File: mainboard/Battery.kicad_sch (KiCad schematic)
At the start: 24 parts, among them IC701 USBLC6-2P6, IC702 BQ21040DBV, IC703 MAX17048, Q701 Si2333CDS, X701 USB, X702 Battery

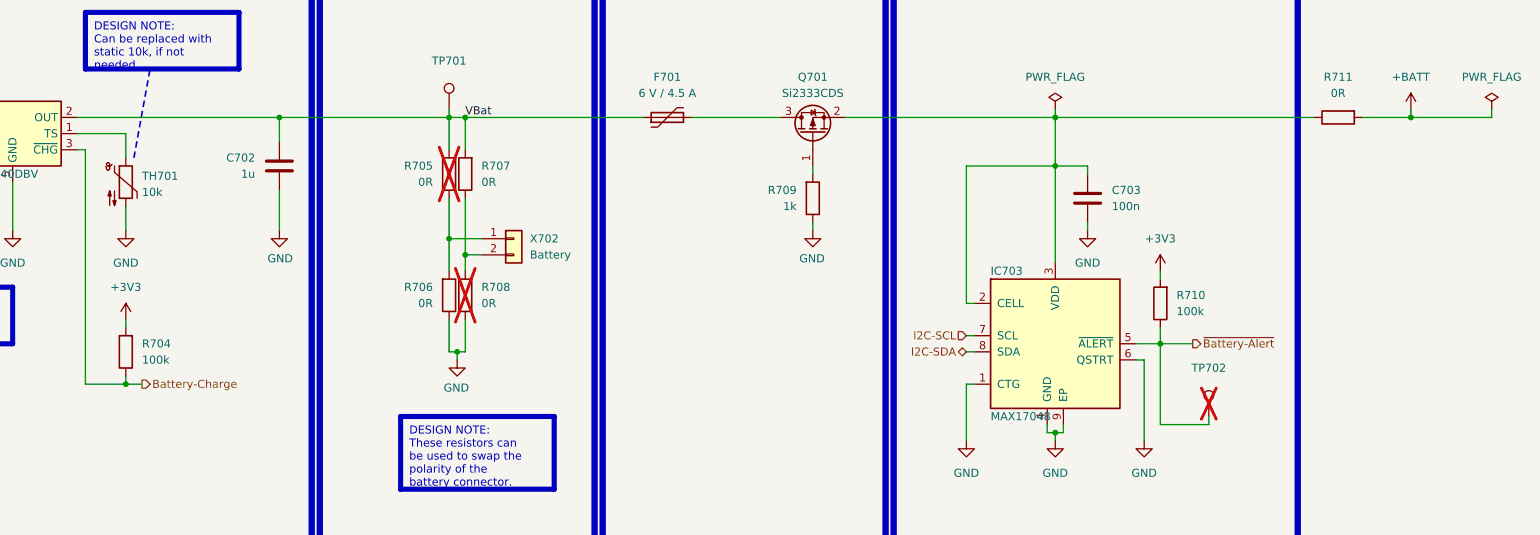
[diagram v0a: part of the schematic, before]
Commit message: Changed: Fix different minor assembly ToDos
Signed-off-by: Daniel Kampert <DanielKampert@kampis-elektroecke.de>
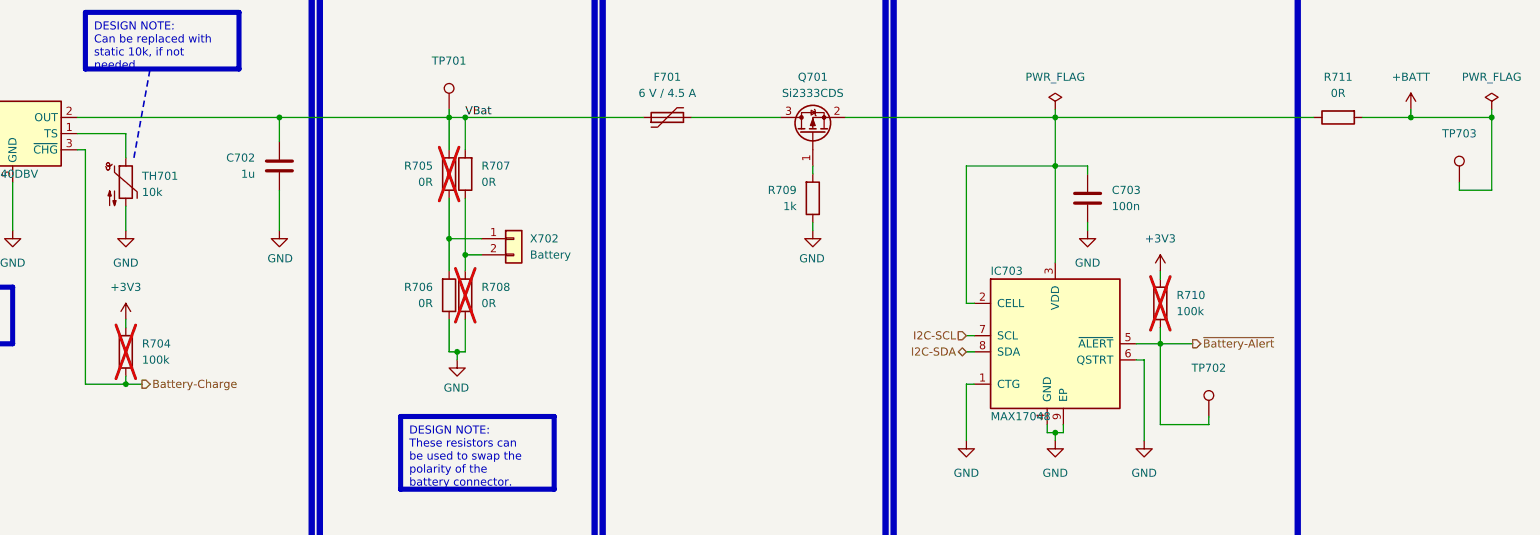
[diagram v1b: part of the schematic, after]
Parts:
- added TP703: ~, Testpoints_Kampi:TestPoint_Pad_1.0x1.0mm, symbol Connector:TestPoint
- R704, R710: now not fitted; now left out of the parts list
- TP702: now fitted
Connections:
- net +BATT: now also TP703.1
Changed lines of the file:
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@@
 	)
 	(junction
+		(at 393.7 109.22)
+		(diameter 0)
+		(color 0 0 0 0)
+	)
+	(junction
 		(at 128.27 109.22)
 		(diameter 0)
@@
 	(wire
 		(pts
+			(xy 388.62 120.65) (xy 393.7 120.65)
+		)
+		(stroke
+			(width 0)
+			(type default)
+		)
+	)
+	(wire
+		(pts
 			(xy 128.27 109.22) (xy 128.27 113.03)
 		)
@@
 	(wire
 		(pts
+			(xy 393.7 120.65) (xy 393.7 109.22)
+		)
+		(stroke
+			(width 0)
+			(type default)
+		)
+	)
+	(wire
+		(pts
 			(xy 292.1 109.22) (xy 325.12 109.22)
 		)
@@
 	(wire
 		(pts
+			(xy 388.62 119.38) (xy 388.62 120.65)
+		)
+		(stroke
+			(width 0)
+			(type default)
+		)
+	)
+	(wire
+		(pts
 			(xy 381 107.95) (xy 381 109.22)
 		)
@@
 	)
 	(symbol
+		(lib_id "Connector:TestPoint")
+		(at 388.62 119.38 0)
+		(unit 1)
+		(exclude_from_sim no)
+		(in_bom no)
+		(on_board yes)
+		(dnp no)
+		(property "Reference" "TP703"
+			(at 388.62 111.76 0)
+			(effects
+				(font
+					(size 1.27 1.27)
+				)
+			)
+		)
+		(property "Value" "~"
+			(at 388.62 113.665 0)
+			(effects
+				(font
+					(size 1.27 1.27)
+				)
+			)
+		)
+		(property "Footprint" "Testpoints_Kampi:TestPoint_Pad_1.0x1.0mm"
+			(at 393.7 119.38 0)
+			(effects
+				(font
+					(size 1.27 1.27)
+				)
+				(hide yes)
+			)
+		)
+		(property "Datasheet" "~"
+			(at 393.7 119.38 0)
+			(effects
+				(font
+					(size 1.27 1.27)
+				)
+				(hide yes)
+			)
+		)
+		(property "Description" "test point"
+			(at 388.62 119.38 0)
+			(effects
+				(font
+					(size 1.27 1.27)
+				)
+				(hide yes)
+			)
+		)
+		(property "manf" ""
+			(at 388.62 119.38 0)
+			(effects
+				(font
+					(size 1.27 1.27)
+				)
+				(hide yes)
+			)
+		)
+		(property "manf#" ""
+			(at 388.62 119.38 0)
+			(effects
+				(font
+					(size 1.27 1.27)
+				)
+				(hide yes)
+			)
+		)
+		(property "mouser#" ""
+			(at 388.62 119.38 0)
+			(effects
+				(font
+					(size 1.27 1.27)
+				)
+				(hide yes)
+			)
+		)
+		(property "CONFIG" ""
+			(at 388.62 119.38 0)
+			(effects
+				(font
+					(size 1.27 1.27)
+				)
+				(hide yes)
+			)
+		)
+		(pin "1"
+		)
+		(instances
+			(project "Mainboard"
+				(path "/d5742f03-3b1a-42e5-a384-018bd4b919aa/c5103ceb-5325-4a84-a025-9638a412984e/a86b9e25-5bc0-455f-833c-d00b4e9a8b22"
+					(reference "TP703")
+					(unit 1)
+				)
+			)
+		)
+	)
+	(symbol
 		(lib_id "power:PWR_FLAG")
 		(at 393.7 107.95 0)
@@
 		(unit 1)
 		(exclude_from_sim no)
-		(in_bom yes)
+		(in_bom no)
 		(on_board yes)
-		(dnp no)
+		(dnp yes)
 		(property "Reference" "R704"
 			(at 181.61 144.7799 0)
@@
 		(unit 1)
 		(exclude_from_sim no)
-		(in_bom yes)
+		(in_bom no)
 		(on_board yes)
-		(dnp no)
+		(dnp yes)
 		(property "Reference" "R710"
 			(at 344.17 137.1599 0)
@@
 		(in_bom no)
 		(on_board yes)
-		(dnp yes)
+		(dnp no)
 		(property "Reference" "TP702"
 			(at 349.25 148.59 0)

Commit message: Update to KiCad 10
Closes: #31, #29, #27

Signed-off-by: Daniel Kampert <DanielKampert@kampis-elektroecke.de>
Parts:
- TP701, TP702, TP703: value ~ -> (none)
